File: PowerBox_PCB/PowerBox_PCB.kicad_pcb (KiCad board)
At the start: 2 copper layers, 120 x 85 mm, 46 parts

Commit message: Added USBPD & BMD & BATTCHARGER
Added USBPD & BMD & BATTCHARGER
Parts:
- added B1: 2S Batt Pack, Custom_Footprints:2S Batt Pack, F.Cu at (52.2, 88.5)
- added C20: 1uF, Capacitor_SMD:C_0805_2012Metric_Pad1.18x1.45mm_HandSolder, F.Cu at (115.3, 62.8)
- added C21: 0.1uF, Capacitor_SMD:C_0805_2012Metric_Pad1.18x1.45mm_HandSolder, F.Cu at (58.7, 84.8)
- added C22: 0.1uF, Capacitor_SMD:C_0805_2012Metric_Pad1.18x1.45mm_HandSolder, F.Cu at (59.2, 95.8)
- added C26: 1uF, Capacitor_SMD:C_0805_2012Metric_Pad1.18x1.45mm_HandSolder, F.Cu at (67.5, 129.0)
- added C27: 10uf, Capacitor_SMD:C_0805_2012Metric_Pad1.18x1.45mm_HandSolder, F.Cu at (57.0, 120.7)
- added C28: 47nF, Capacitor_SMD:C_0805_2012Metric_Pad1.18x1.45mm_HandSolder, F.Cu at (57.2, 108.5)
- added C29: 44uF, Capacitor_SMD:C_0805_2012Metric_Pad1.18x1.45mm_HandSolder, F.Cu at (55.2, 116.5)
- added C30: 10uf, Capacitor_SMD:C_0805_2012Metric_Pad1.18x1.45mm_HandSolder, F.Cu at (55.2, 114.2)
- added ID2: 1uh, Inductor_SMD:L_1008_2520Metric_Pad1.43x2.20mm_HandSolder, F.Cu at (54.0, 120.4)
- added L4: LED, LED_SMD:LED_0805_2012Metric_Pad1.15x1.40mm_HandSolder, F.Cu at (67.5, 124.7)
- added R19: 1kΩ, Resistor_SMD:R_0805_2012Metric_Pad1.20x1.40mm_HandSolder, F.Cu at (67.7, 83.5)
- added R22: 100Ω, Resistor_SMD:R_0805_2012Metric_Pad1.20x1.40mm_HandSolder, F.Cu at (56.5, 84.8)
- added R23: 100Ω, Resistor_SMD:R_0805_2012Metric_Pad1.20x1.40mm_HandSolder, F.Cu at (57.0, 93.5)
- added R24: 1kΩ, Resistor_SMD:R_0805_2012Metric_Pad1.20x1.40mm_HandSolder, F.Cu at (67.5, 95.5)
- added R26: 49.9kΩ, Resistor_SMD:R_0805_2012Metric_Pad1.20x1.40mm_HandSolder, F.Cu at (103.8, 63.0)
- added R27: 5.1kΩ, Resistor_SMD:R_0805_2012Metric_Pad1.20x1.40mm_HandSolder, F.Cu at (110.6, 67.3)
- added R28: 10Ω, Resistor_SMD:R_0805_2012Metric_Pad1.20x1.40mm_HandSolder, F.Cu at (118.1, 62.8)
- added R29: 6.04Ω, Resistor_SMD:R_0805_2012Metric_Pad1.20x1.40mm_HandSolder, F.Cu at (106.8, 63.0)
- added R31: 10kΩ, Resistor_SMD:R_0805_2012Metric_Pad1.20x1.40mm_HandSolder, F.Cu at (68.8, 112.0)
- added R32: 10kΩ, Resistor_SMD:R_0805_2012Metric_Pad1.20x1.40mm_HandSolder, F.Cu at (68.8, 114.2)
- added R33: 10kΩ, Resistor_SMD:R_0805_2012Metric_Pad1.20x1.40mm_HandSolder, F.Cu at (68.8, 116.5)
- added R34: 10kΩ, Resistor_SMD:R_0805_2012Metric_Pad1.20x1.40mm_HandSolder, F.Cu at (68.8, 119.5)
- added R36: 5.23kΩ, Capacitor_SMD:C_0805_2012Metric_Pad1.18x1.45mm_HandSolder, F.Cu at (77.0, 117.2)
- added R37: 383Ω, Capacitor_SMD:C_0805_2012Metric_Pad1.18x1.45mm_HandSolder, F.Cu at (68.8, 109.7)
- added R38: 30.1kΩ, Capacitor_SMD:C_0805_2012Metric_Pad1.18x1.45mm_HandSolder, F.Cu at (77.0, 119.5)
- added R39: 10Ω_2W, Resistor_SMD:R_2512_6332Metric_Pad1.40x3.35mm_HandSolder, F.Cu at (61.0, 108.5)
- added R40: 300Ω, Resistor_SMD:R_0805_2012Metric_Pad1.20x1.40mm_HandSolder, F.Cu at (64.8, 108.2)
- added R41: 2.2kΩ, Resistor_SMD:R_0805_2012Metric_Pad1.20x1.40mm_HandSolder, F.Cu at (69.8, 124.7)
- added TR1: 10kΩ, Custom_Footprints:ThermistorPads, F.Cu at (77.0, 125.2)
- added U10: BQ25887RGER, BQ25887RGER:VQFN24_RGE_TEX, F.Cu at (61.2, 116.2)
- added U11: ~, Package_TO_SOT_SMD:SOT-23-6_Handsoldering, F.Cu at (63.3, 83.3)
- added U13: ~, Package_TO_SOT_SMD:SOT-23_Handsoldering, F.Cu at (63.4, 89.5)
- added U14: ~, Package_TO_SOT_SMD:SOT-23_Handsoldering, F.Cu at (67.7, 89.5)
- added U15: ~, Package_TO_SOT_SMD:SOT-23-6_Handsoldering, F.Cu at (63.4, 94.5)
- added U16: ~, Package_TO_SOT_SMD:SOT-23_Handsoldering, F.Cu at (63.2, 100.2)
- added U17: ~, Package_TO_SOT_SMD:SOT-23_Handsoldering, F.Cu at (67.5, 100.2)
- added U18: ~, Package_TO_SOT_SMD:TO-252-3_TabPin2, F.Cu at (62.0, 126.7)
- added U20: ~, Custom_Footprints:DFN-10_L3.0-W3.0-P0.50-BL-EP2.5, F.Cu at (110.6, 63.2)
- added U21: ~, Package_TO_SOT_SMD:SOT-223, F.Cu at (97.8, 65.8)
- added USBC2: ~, Custom_Footprints:USB-C_SMD-TYPE-C-31-M-12_1, F.Cu at (110.0, 54.2)
- moved R7 15.7 mm to (124.6, 88.2)
- moved R8 15.7 mm to (116.6, 88.4)
- moved U4 15.7 mm to (120.6, 88.7)
- moved C1 15.7 mm to (96.2, 79.6)
- moved C2 15.7 mm to (104.4, 76.6)
- moved C3 15.7 mm to (88.6, 89.8)
- moved C4 15.7 mm to (77.6, 84.0)
- moved C5 15.7 mm to (80.6, 84.0)
- moved C6 15.7 mm to (83.6, 84.0)
- moved C7 15.7 mm to (92.4, 87.8)
- moved C8 15.7 mm to (92.4, 89.8)
- moved C9 15.7 mm to (92.4, 91.8)
- moved L1 15.7 mm to (104.6, 83.7)
- moved R1 15.7 mm to (104.4, 91.6)
- moved R17 15.7 mm to (108.0, 96.4)
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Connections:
- net /TPS54620_Buck/VIN_BUCK renamed VUSBPD
- net /TPS54620_Buck1/VIN_BUCK renamed P+
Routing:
- net P+: track 0.00 -> 133.2 mm
- net VUSBPD: track 0.00 -> 95.8 mm, vias 0 -> 12
- net /Batt Charger/TS: track 0.00 -> 34.9 mm
- net PM: track 0.00 -> 34.6 mm
- net /USBPD/VBUS: track 0.00 -> 33.8 mm, vias 0 -> 7
- net Net-(U10-REGN): track 0.00 -> 29.0 mm
- net /BMS/BM: track 0.00 -> 19.7 mm
- net /Batt Charger/VOUT: track 0.00 -> 17.6 mm
- net Net-(U11-OC): track 0.00 -> 17.5 mm
- net /BMS/B-: track 0.00 -> 16.5 mm
- net Net-(U15-OC): track 0.00 -> 15.9 mm
- net GND: track 1.00 -> 16.7 mm, vias 6 -> 27
- net /Batt Charger/SW: track 0.00 -> 14.9 mm, vias 0 -> 2
- net /USBPD/D+: track 0.00 -> 11.7 mm, vias 0 -> 2
- net Net-(U10-STAT): track 0.00 -> 11.6 mm
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- added copper zone on B.Cu, net /USBPD/VBUS
- added copper zone on B.Cu, net GND

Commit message: Finished
Basically done
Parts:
- added SW1: SW_DPDT_x2, Custom_Footprints:SwitchPads, F.Cu at (86.2, 79.0)
- added TP1: ~, Custom_Footprints:PAD-2x2, F.Cu at (92.0, 69.0)
- added TP10: ~, Custom_Footprints:PAD-2x2, F.Cu at (166.8, 98.5)
- added TP11: ~, Custom_Footprints:PAD-2x2, F.Cu at (87.8, 99.8)
- added TP12: ~, Custom_Footprints:PAD-2x2, F.Cu at (135.2, 94.0)
- added TP13: ~, Custom_Footprints:PAD-2x2, F.Cu at (134.8, 70.5)
- added TP14: ~, Custom_Footprints:M3-Pad, F.Cu at (53.8, 53.8)
- added TP15: ~, Custom_Footprints:M3-Pad, F.Cu at (166.2, 53.8)
- added TP16: ~, Custom_Footprints:M3-Pad, F.Cu at (53.8, 131.2)
- added TP17: ~, Custom_Footprints:M3-Pad, F.Cu at (166.2, 131.2)
- added TP2: ~, Custom_Footprints:PAD-2x2, F.Cu at (52.2, 101.8)
- added TP3: ~, Custom_Footprints:PAD-2x2, F.Cu at (54.2, 79.8)
- added TP4: ~, Custom_Footprints:PAD-2x2, F.Cu at (71.0, 88.0)
- added TP5: ~, Custom_Footprints:PAD-2x2, F.Cu at (105.5, 106.8)
- added TP6: ~, Custom_Footprints:PAD-2x2, F.Cu at (166.8, 91.2)
- added TP7: ~, Custom_Footprints:PAD-2x2, F.Cu at (105.5, 82.2)
- added TP8: ~, Custom_Footprints:PAD-2x2, F.Cu at (166.8, 88.2)
- added TP9: ~, Custom_Footprints:PAD-2x2, F.Cu at (166.8, 95.5)
- moved C30 43.1 mm to (98.0, 119.5), turned to 0 degrees
- moved ID2 42.3 mm to (95.7, 113.3), turned to -90 degrees
- moved C29 39.2 mm to (94.5, 117.2), turned to 0 degrees
- moved C28 39.0 mm to (92.5, 125.2), turned to 90 degrees
- moved C27 36.5 mm to (92.7, 113.0), turned to 90 degrees
- moved U18 32.5 mm to (87.7, 106.9), turned to 90 degrees
- moved R39 32.4 mm to (88.7, 125.2), turned to 90 degrees
- moved C26 28.4 mm to (82.2, 104.7), turned to -90 degrees
- moved U10 27.3 mm to (88.5, 117.5), turned to 0 degrees
- moved R40 26.5 mm to (85.0, 125.4), turned to 90 degrees
- moved U7 22.6 mm to (138.5, 101.1)
- moved C1 22.6 mm to (118.1, 74.1)
- moved C10 22.6 mm to (105.5, 102.8)
- moved C12 22.6 mm to (99.5, 102.8)
- moved C13 22.6 mm to (110.5, 108.6)
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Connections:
- C10 pad 1: P+ -> /TPS54620_Buck1/VIN_BUCK
- C11 pad 1: P+ -> /TPS54620_Buck1/VIN_BUCK
- C12 pad 1: P+ -> /TPS54620_Buck1/VIN_BUCK
- C13 pad 1: P+ -> /TPS54620_Buck1/VIN_BUCK
- C3 pad 1: VUSBPD -> /VUSBPDSWITCHED
- C4 pad 1: VUSBPD -> /VUSBPDSWITCHED
- C5 pad 1: VUSBPD -> /VUSBPDSWITCHED
- C6 pad 1: VUSBPD -> /VUSBPDSWITCHED
- R3 pad 1: VUSBPD -> /VUSBPDSWITCHED
- R9 pad 1: P+ -> /TPS54620_Buck1/VIN_BUCK
- U1 pad 4: VUSBPD -> /VUSBPDSWITCHED
- U1 pad 5: VUSBPD -> /VUSBPDSWITCHED
- U1 pad 6: VUSBPD -> /VUSBPDSWITCHED
- U18 pad 3: VUSBPD -> /VUSBPDSWITCHED
- U5 pad 4: P+ -> /TPS54620_Buck1/VIN_BUCK
- U5 pad 5: P+ -> /TPS54620_Buck1/VIN_BUCK
- U5 pad 6: P+ -> /TPS54620_Buck1/VIN_BUCK
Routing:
- net /VUSBPDSWITCHED: track 0.00 -> 67.6 mm, vias 0 -> 9
- net VUSBPD: track 95.8 -> 30.1 mm, vias 12 -> 0
- net /Ideal_Diode/VOUT_IDEAL: track 11.7 -> 74.3 mm
- net PM: track 34.6 -> 68.7 mm
- net /TPS54620_Buck1/VIN_BUCK: track 0.00 -> 27.2 mm
- net P+: track 133.2 -> 120.8 mm, vias 0 -> 12
- net /Ideal_Diode1/VIN_IDEAL: track 17.5 -> 23.9 mm
- net /Ideal_Diode/VIN_IDEAL: track 30.3 -> 36.6 mm
- net /Batt Charger/VOUT: track 17.6 -> 23.5 mm
- added copper zone on F.Cu, net /TPS54620_Buck1/VIN_BUCK
- added copper zone on F.Cu, net /VUSBPDSWITCHED
- removed copper zone on F.Cu, net P+
- removed copper zone on F.Cu, net VUSBPD
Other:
- board size 120 x 85 mm -> 383 x 91 mm
- board text added: "+"
- board text added: "-"
- board text added: "GND"
- board text added: "M"
- board text added: "VOUT"

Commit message: e
e
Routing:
- net Net-(C17-Pad2): vias 0 -> 11
- net Net-(C1-Pad2): vias 0 -> 11
- net GND: vias 27 -> 57
- net /VUSBPDSWITCHED: vias 9 -> 12
- net /TPS54620_Buck1/VIN_BUCK: vias 0 -> 3
- net /Ideal_Diode1/VIN_IDEAL: vias 0 -> 8
- net /Ideal_Diode/VIN_IDEAL: vias 0 -> 8
- added copper zone on B.Cu, net /Ideal_Diode/VIN_IDEAL
- added copper zone on B.Cu, net /Ideal_Diode1/VIN_IDEAL
- added copper zone on B.Cu, net /TPS54620_Buck1/VIN_BUCK
- added copper zone on B.Cu, net /VUSBPDSWITCHED
- added copper zone on B.Cu, net Net-(C1-Pad2)
- added copper zone on B.Cu, net Net-(C17-Pad2)
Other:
- board size 383 x 91 mm -> 120 x 85 mm
- board text added: "© CC-BY-NC-SA 4.0 Alvin Alford PowerBox, an all in one power solution for a cyberdeck or other portable project. Powered by 2 lithium (lipo or lion) cells for up to 36 Ws of power"

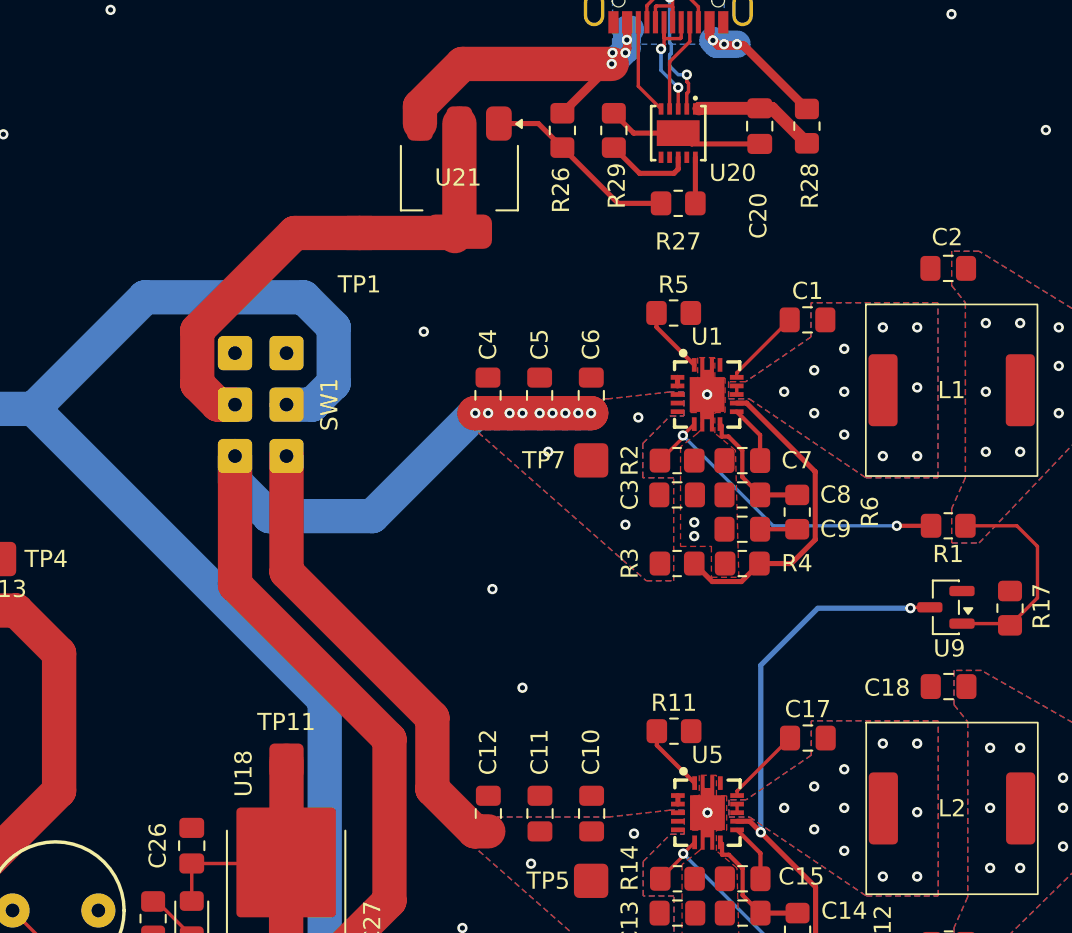
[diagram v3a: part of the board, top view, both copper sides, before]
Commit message: add indicator lights
add indicator lights
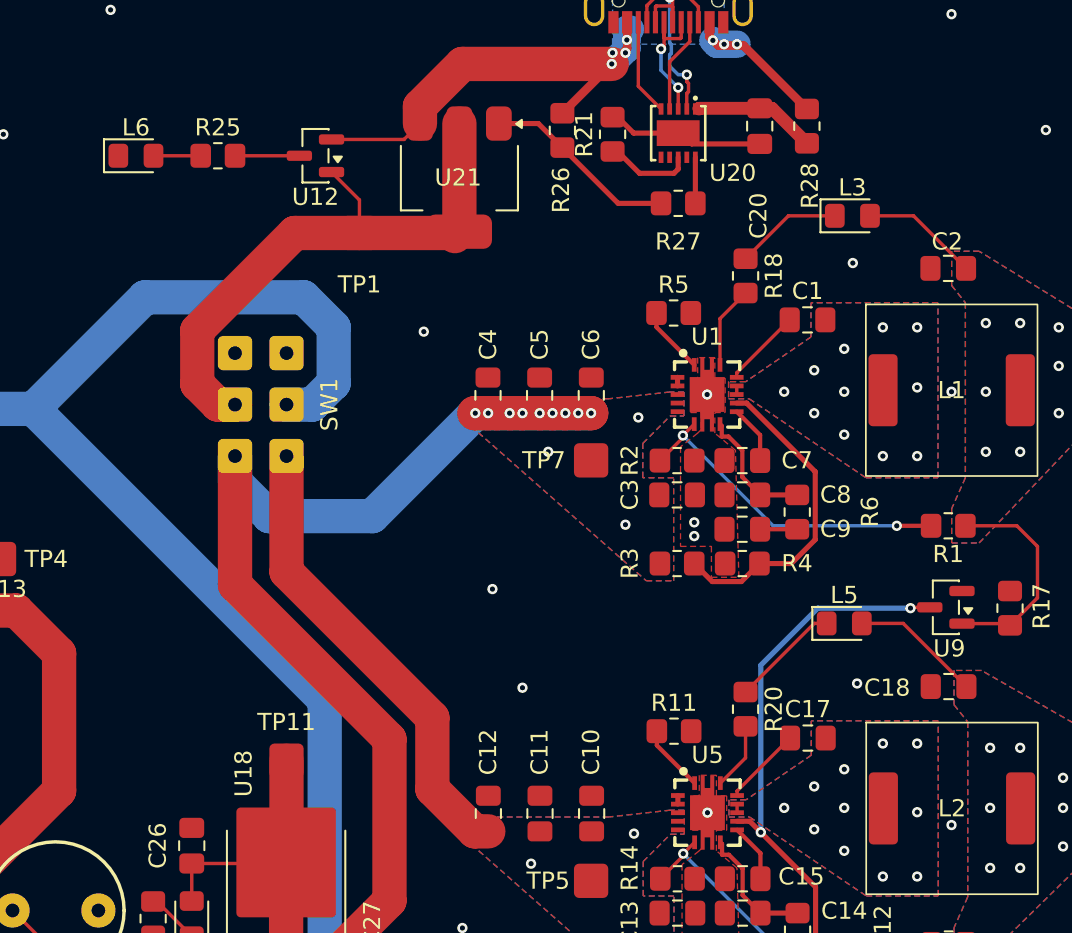
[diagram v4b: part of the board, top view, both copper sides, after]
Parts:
- removed R29: 6.04Ω, Resistor_SMD:R_0805_2012Metric_Pad1.20x1.40mm_HandSolder
- added L3: LED, LED_SMD:LED_0805_2012Metric_Pad1.15x1.40mm_HandSolder, F.Cu at (120.7, 68.0)
- added L5: LED, LED_SMD:LED_0805_2012Metric_Pad1.15x1.40mm_HandSolder, F.Cu at (120.2, 91.8)
- added L6: LED, LED_SMD:LED_0805_2012Metric_Pad1.15x1.40mm_HandSolder, F.Cu at (79.0, 64.5)
- added R18: 1kΩ, Resistor_SMD:R_0805_2012Metric_Pad1.20x1.40mm_HandSolder, F.Cu at (114.5, 71.5)
- added R20: 1kΩ, Resistor_SMD:R_0805_2012Metric_Pad1.20x1.40mm_HandSolder, F.Cu at (114.5, 96.8)
- added R21: 10Ω, Resistor_SMD:R_0805_2012Metric_Pad1.20x1.40mm_HandSolder, F.Cu at (106.8, 63.2)
- added R25: 1kΩ, Resistor_SMD:R_0805_2012Metric_Pad1.20x1.40mm_HandSolder, F.Cu at (83.8, 64.5)
- added U12: ~, Package_TO_SOT_SMD:SOT-23, F.Cu at (89.4, 64.5)
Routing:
- net /Ideal_Diode1/VIN_IDEAL: track 23.9 -> 31.6 mm
- net /Ideal_Diode/VIN_IDEAL: track 36.6 -> 43.5 mm
- net Net-(L5-K): track 0.00 -> 6.38 mm
- net Net-(L3-K): track 0.00 -> 6.24 mm
- net /USBPD/VBUS: track 33.8 -> 39.3 mm
- net /TPS54620_Buck/PWRGD_BUCK: track 0.00 -> 4.80 mm
- net VUSBPD: track 30.1 -> 34.4 mm
- net /TPS54620_Buck1/PWRGD_BUCK: track 0.00 -> 3.91 mm
- net Net-(U12-C): track 0.00 -> 3.75 mm
- net Net-(L6-A): track 0.00 -> 2.75 mm
- net GND: vias 57 -> 61
